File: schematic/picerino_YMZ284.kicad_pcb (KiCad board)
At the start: 2 copper layers, 83.8 x 53.5 mm, 23 parts, among them CON1 PICERINO-EDGE, J1 Conn_01x02, J2 Conn_01x02, J3 Conn_01x02, U1 YMZ284, U2 74LS00, U3 LM386, Y1 3.579545Mhz

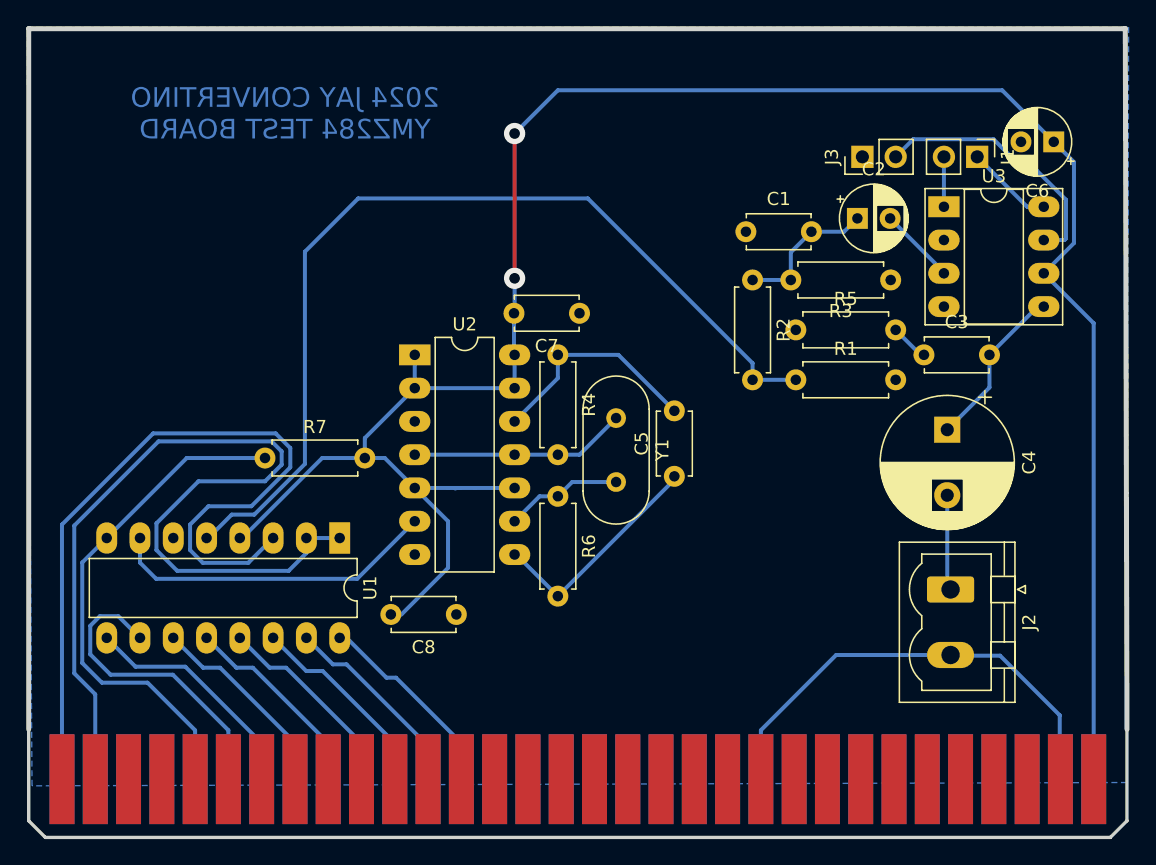
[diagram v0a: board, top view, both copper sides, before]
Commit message: first version with library conversion. main test app still needs to be converted
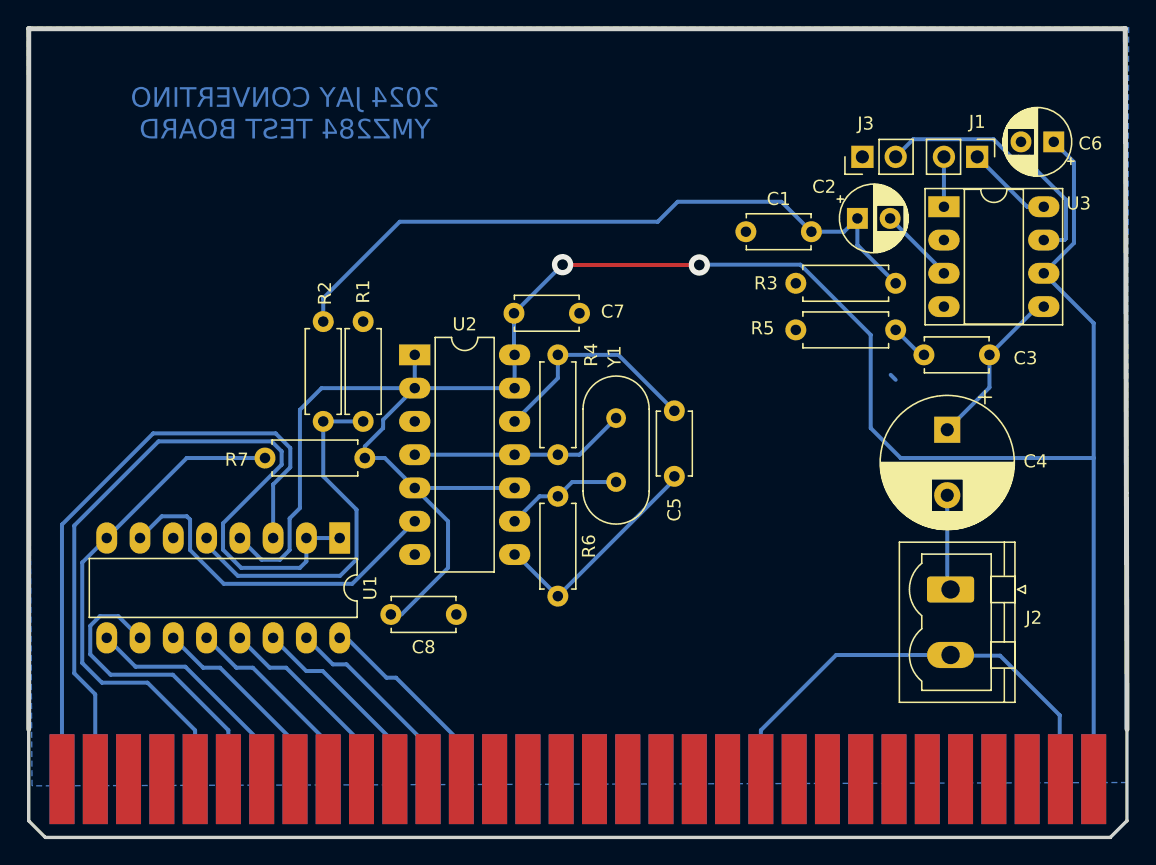
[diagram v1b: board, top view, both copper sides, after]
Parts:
- moved R1 33.2 mm to (132.5, 80.6), turned to 90 degrees
- moved R2 32.9 mm to (129.4, 73.0)
- moved R3 7.24 mm to (165.5, 70.1), turned to 0 degrees
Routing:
- net Net-(U1-OUT): track 71.7 -> 28.1 mm
- net Net-(C1-Pad2): track 11.2 -> 53.1 mm
- net Net-(U1-A0): track 60.6 -> 47.6 mm
- net VCC: track 170.2 -> 181.6 mm
- net Net-(U1-~{CS}): track 69.6 -> 59.6 mm
- net Net-(U1-CLK): track 25.2 -> 27.1 mm
